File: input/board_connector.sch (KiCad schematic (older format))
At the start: 6 parts, among them J2 C64AB, J3 Decimate

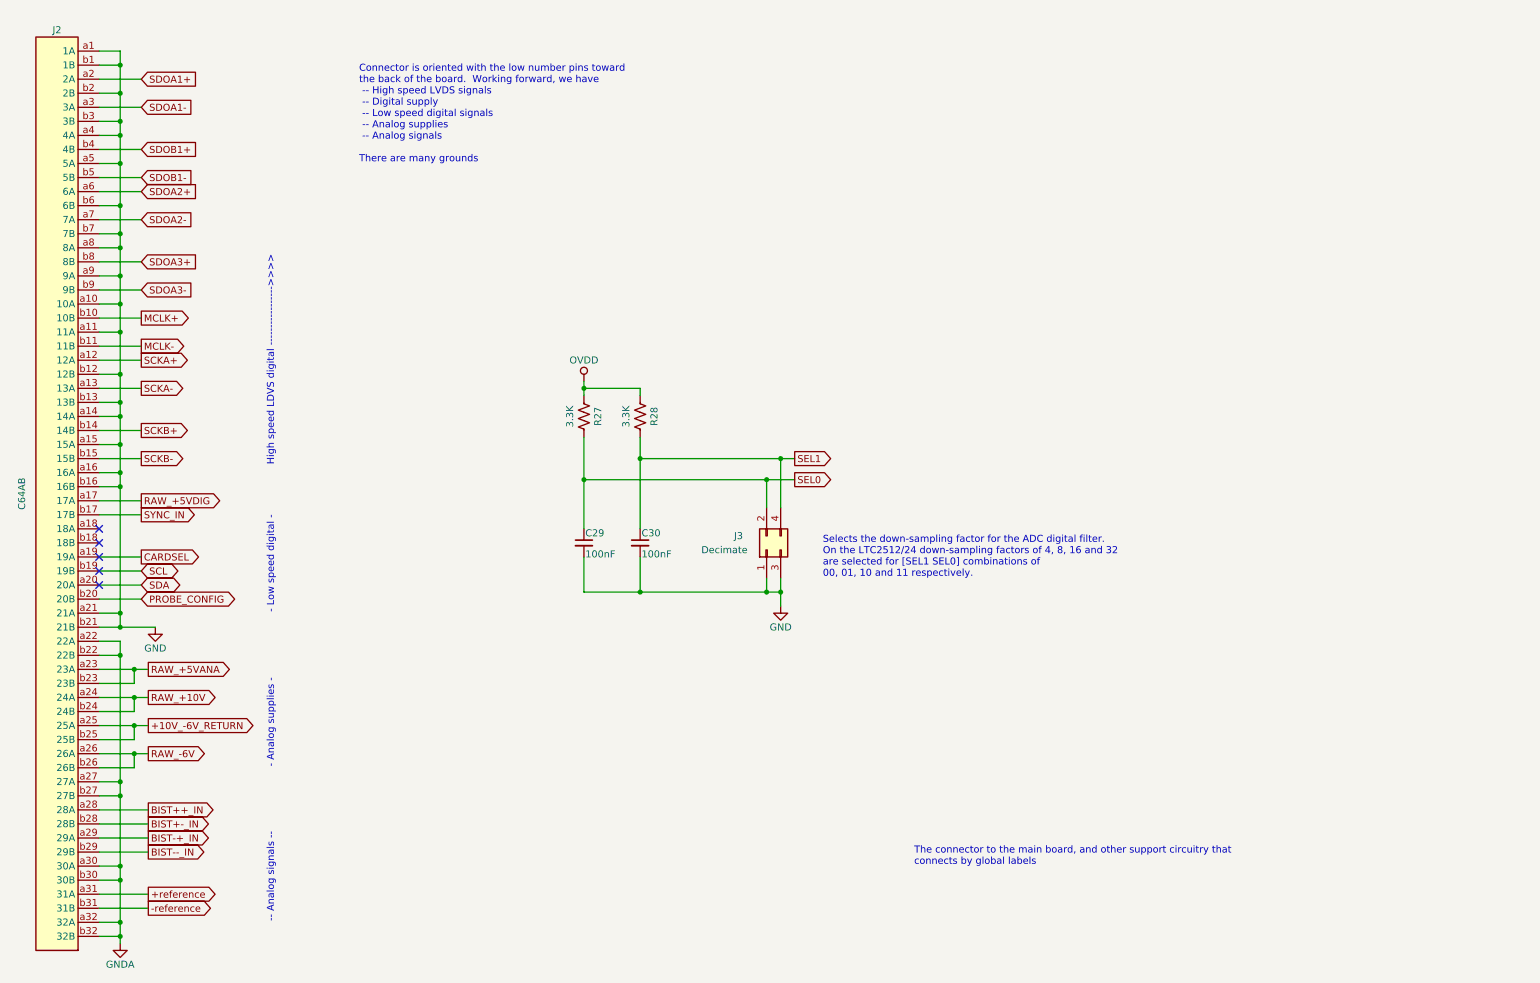
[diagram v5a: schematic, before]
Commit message: Changed board connector to PCIe 8x, added test points, cleanup of component values. Add LVDS Rx termination, bypass caps.
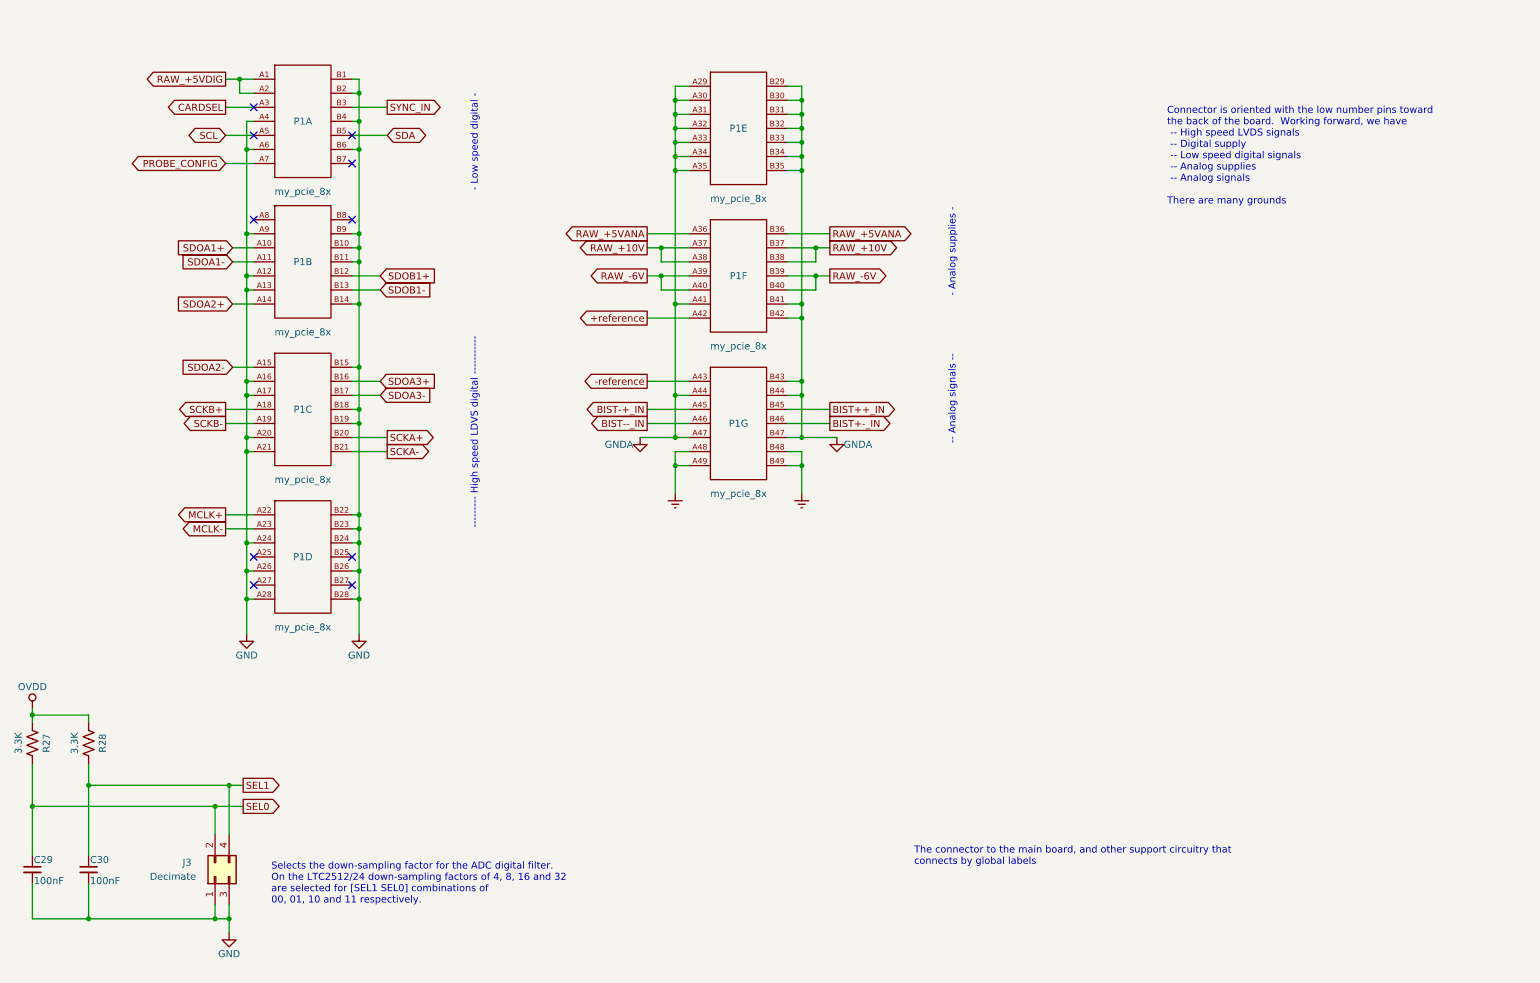
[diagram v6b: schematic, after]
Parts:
- removed J2: C64AB, Connector_DIN:DIN41612_B_2x32_Horizontal, symbol ilemt_input:my_C64AB
- added P1: my_pcie_8x, input:BUS_PCIexpress_x8, symbol ilemt_input:my_pcie_8x
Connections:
- net +reference: now also P1.A42
- net -reference: now also P1.A43
- net BIST++_IN: now also P1.B45
- net BIST+-_IN: now also P1.B46
- net BIST-+_IN: now also P1.A45
- net BIST--_IN: now also P1.A46
- net CARDSEL: now also P1.A3
- net GND: now also P1.A12, P1.A13, P1.A16, P1.A17, P1.A20, P1.A21, P1.A24, P1.A26, P1.A28, P1.A4, P1.A6, P1.A9, P1.B1, P1.B10, P1.B11, P1.B14, P1.B15, P1.B18, P1.B19, P1.B2, P1.B22, P1.B23, P1.B24, P1.B26, P1.B28, P1.B4, P1.B6, P1.B9
- net GNDA: now also P1.A29, P1.A30, P1.A31, P1.A32, P1.A33, P1.A34, P1.A35, P1.A41, P1.A44, P1.A47, P1.B29, P1.B30, P1.B31, P1.B32, P1.B33, P1.B34, P1.B35, P1.B41, P1.B42, P1.B43, P1.B44, P1.B47
- net MCLK+: now also P1.A22
- net MCLK-: now also P1.A23
- net PROBE_CONFIG: now also P1.A7
- net RAW_+10V: now also P1.A37, P1.A38, P1.B37, P1.B38
- net RAW_+5VANA: now also P1.A36, P1.B36
- net RAW_+5VDIG: now also P1.A1, P1.A2
- net RAW_-6V: now also P1.A39, P1.A40, P1.B39, P1.B40
- net SCKA+: now also P1.B20
- net SCKA-: now also P1.B21
- net SCKB+: now also P1.A18
- net SCKB-: now also P1.A19
- net SCL: now also P1.A5
- net SDA: now also P1.B5
- net SDOA1+: now also P1.A10
- net SDOA1-: now also P1.A11
- net SDOA2+: now also P1.A14
- net SDOA2-: now also P1.A15
- net SDOA3+: now also P1.B16
- net SDOA3-: now also P1.B17
- net SDOB1+: now also P1.B12
- net SDOB1-: now also P1.B13
- net SYNC_IN: now also P1.B3
- new net Earth: P1.A48 (A47), P1.A49, P1.B48, P1.B49
- no-connect marks 5 -> 10
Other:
- note added: "--------- High speed LDVS digital -----------"
- note removed: "High speed LDVS digital ----------------->>>>"
- moved on the sheet: C29, C30, J3, R27, R28

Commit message: Checkpoint before starting routing.  Added power and ground testpoints.
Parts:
- C29, C30: DK line (none) -> 2; Description (none) -> CAP CER 0.1UF 25V X7R 0603; Digikey (none) -> 311-1341-1-ND
- J3: DK line (none) -> 32
- R27, R28: DK line (none) -> 53; Description (none) -> 3.3 kOhms ±1% 0.1W, 1/10W Chip Resistor 0603 (1608 Metric) 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; Digikey (none) -> YAG3354CT-ND
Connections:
- net +reference renamed VREF+
- net -reference renamed VREF-
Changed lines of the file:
@@
 EESchema Schematic File Version 4
-LIBS:input_board-cache
-EELAYER 29 0
+EELAYER 30 0
 EELAYER END
 $Descr A4 11693 8268
@@
 SDOA2+
 Text GLabel 5350 2900 0    50   Output ~ 0
-+reference
+VREF+
 Text GLabel 5350 3350 0    50   Output ~ 0
--reference
+VREF-
 Text GLabel 3500 1400 2    50   Output ~ 0
 SYNC_IN
@@
 F 2 "Resistor_SMD:R_0603_1608Metric" V 1015 5915 50  0001 C CNN
 F 3 "~" H 975 5925 50  0001 C CNN
+F 4 "53" H 975 5925 50  0001 C CNN "DK line"
+F 5 "3.3 kOhms ±1% 0.1W, 1/10W Chip Resistor 0603 (1608 Metric)  Thin Film" H 975 5925 50  0001 C CNN "Description"
+F 6 "YAG3354CT-ND" H 975 5925 50  0001 C CNN "Digikey"
 	1    975  5925
 	1    0    0    -1
@@
 F 2 "Resistor_SMD:R_0603_1608Metric" V 1415 5915 50  0001 C CNN
 F 3 "~" H 1375 5925 50  0001 C CNN
+F 4 "53" H 1375 5925 50  0001 C CNN "DK line"
+F 5 "3.3 kOhms ±1% 0.1W, 1/10W Chip Resistor 0603 (1608 Metric)  Thin Film" H 1375 5925 50  0001 C CNN "Description"
+F 6 "YAG3354CT-ND" H 1375 5925 50  0001 C CNN "Digikey"
 	1    1375 5925
 	1    0    0    -1
@@
 F 4 "CONN HEADER SMD 4POS 2MM" H 2275 6875 50  0001 C CNN "Description"
 F 5 "S6009-02-ND" H 2275 6875 50  0001 C CNN "Digikey"
+F 6 "32" H 2275 6875 50  0001 C CNN "DK line"
 	1    2275 6875
 	0    -1   -1   0
@@
 F 2 "Capacitor_SMD:C_0603_1608Metric" H 975 6825 50  0001 C CNN
 F 3 "~" H 975 6825 50  0001 C CNN
+F 4 "CAP CER 0.1UF 25V X7R 0603" H 975 6825 50  0001 C CNN "Description"
+F 5 "311-1341-1-ND" H 975 6825 50  0001 C CNN "Digikey"
+F 6 "2" H 975 6825 50  0001 C CNN "DK line"
 	1    975  6825
 	1    0    0    -1
@@
 F 2 "Capacitor_SMD:C_0603_1608Metric" H 1375 6825 50  0001 C CNN
 F 3 "~" H 1375 6825 50  0001 C CNN
+F 4 "CAP CER 0.1UF 25V X7R 0603" H 1375 6825 50  0001 C CNN "Description"
+F 5 "311-1341-1-ND" H 1375 6825 50  0001 C CNN "Digikey"
+F 6 "2" H 1375 6825 50  0001 C CNN "DK line"
 	1    1375 6825
 	1    0    0    -1
